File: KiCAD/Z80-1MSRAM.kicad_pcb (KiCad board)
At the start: 2 copper layers, 100 x 75 mm, 36 parts, among them J1 SBC8080 BUS, J2 I/O ADDR SEL, J3 MSX SLOT, Q1 2SC1815, U1 74HC02, U2 74HC74, U3 74HC139, U4 74HC04, U5 74HC00, U6 628128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

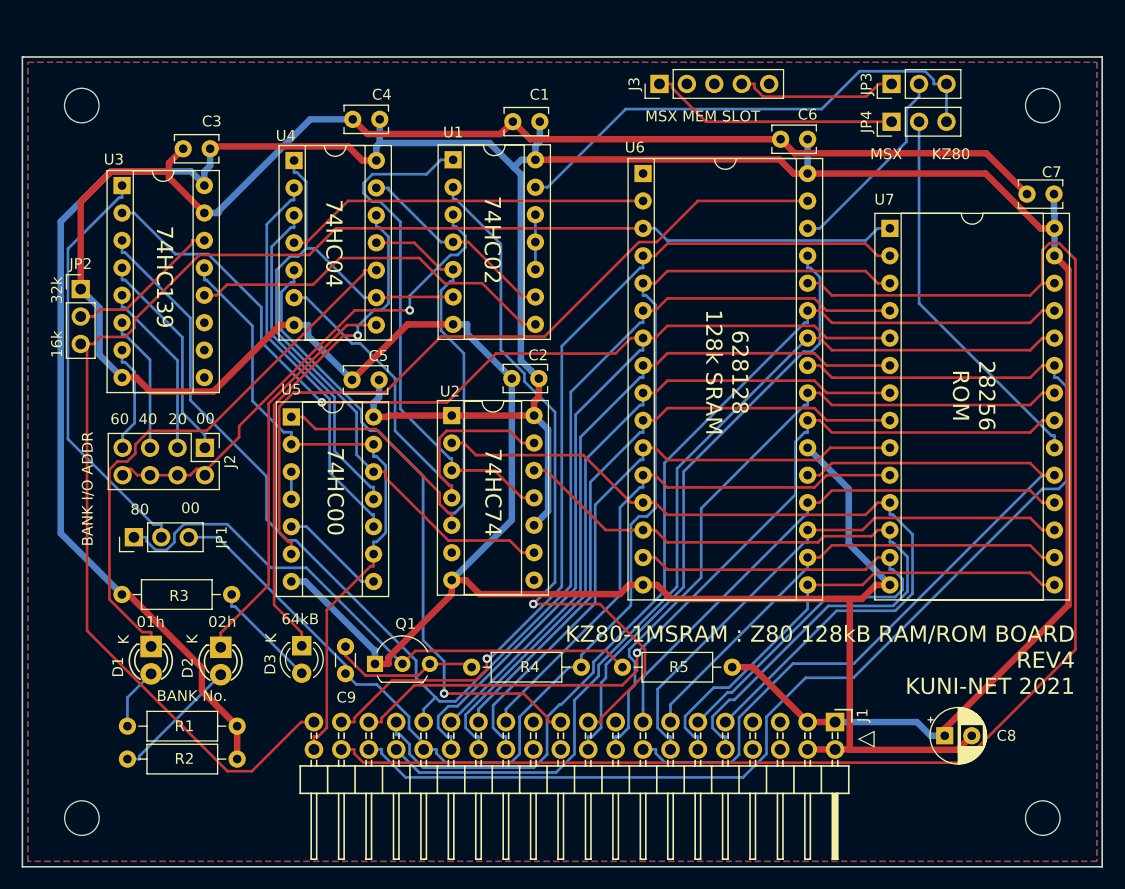
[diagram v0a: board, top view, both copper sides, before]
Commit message: REV4 基板 部品配置変更・ガーバー出力
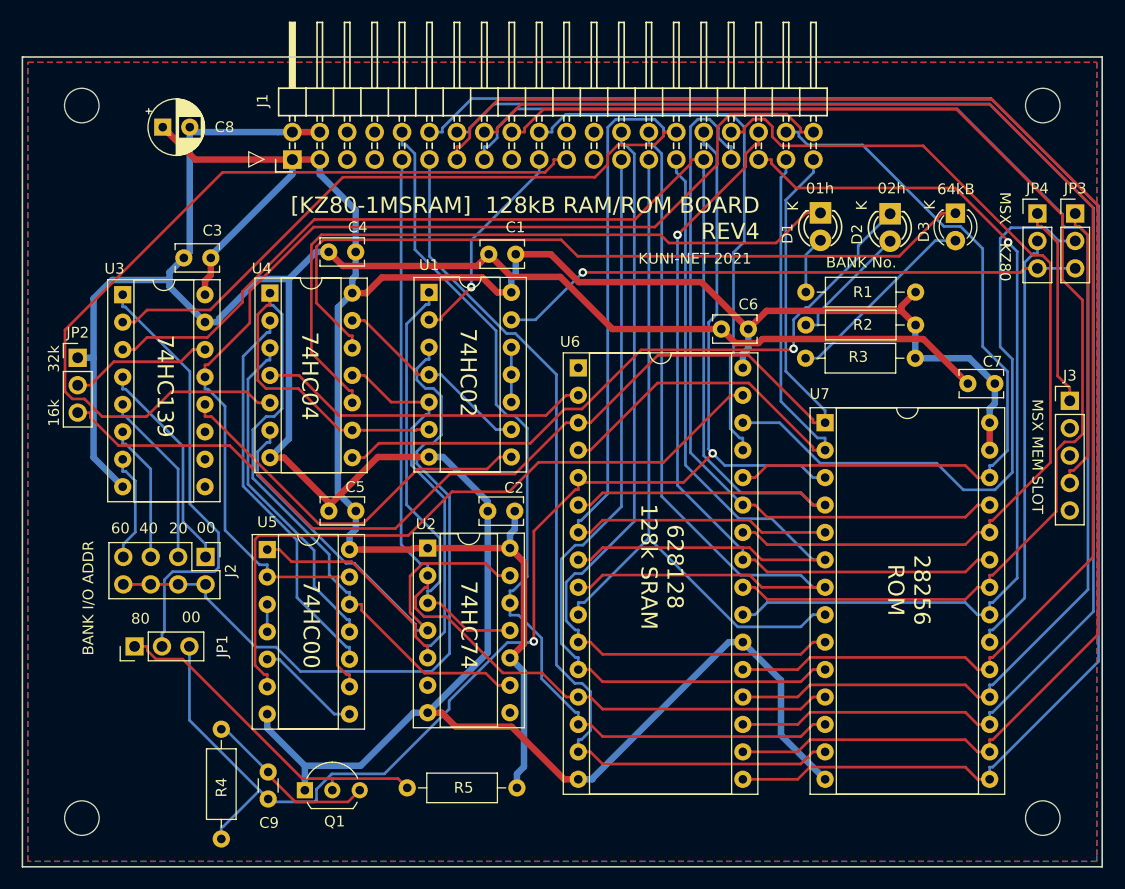
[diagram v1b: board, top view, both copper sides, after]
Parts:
- moved C8 91.8 mm to (113.0, 66.5)
- moved R3 76.7 mm to (182.7, 87.9), turned to 180 degrees
- moved R1 74.6 mm to (182.7, 81.8)
- moved R2 74.6 mm to (182.7, 84.8)
- moved D1 73.9 mm to (173.9, 74.4)
- moved D2 73.9 mm to (180.4, 74.5)
- moved D3 72.6 mm to (186.4, 74.5)
- moved J1 72.4 mm to (125.0, 69.5), turned to 90 degrees
- moved J3 48.0 mm to (197.0, 91.8), turned to 0 degrees
- moved R4 23.9 mm to (118.4, 122.3), turned to 270 degrees
- moved R5 22.9 mm to (135.6, 127.7)
- moved JP3 20.8 mm to (197.5, 74.5), turned to 0 degrees
- moved U6 19.0 mm to (151.5, 88.8)
- moved U7 19.0 mm to (174.3, 93.9)
- moved C6 18.4 mm to (167.2, 85.2)
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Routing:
- net /D3: track 45.3 -> 148.8 mm
- net VCC: track 301.2 -> 198.0 mm
- net /D4: track 44.4 -> 145.7 mm
- net /D5: track 50.7 -> 140.0 mm
- net /D6: track 50.5 -> 135.0 mm
- net /A13: track 140.0 -> 69.7 mm
- net /D7: track 75.6 -> 132.3 mm
- net ~MEMRD: track 65.0 -> 119.4 mm
- net /A15: track 60.0 -> 111.7 mm
- net ~IOWR: track 65.2 -> 19.7 mm
- net /A11: track 114.4 -> 69.4 mm, vias 0 -> 1
- net Net-(JP3-Pad2): track 18.3 -> 58.2 mm
- net /D2: track 51.5 -> 86.3 mm
- net /A12: track 84.1 -> 57.4 mm, vias 1 -> 0
- net Net-(D3-Pad1): track 47.1 -> 72.6 mm, vias 1 -> 0
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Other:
- board text added: "KUNI-NET 2021"
- board text added: "[KZ80-1MSRAM] 128kB RAM/ROM BOARD REV4"
- board text removed: "KZ80-1MSRAM : Z80 128kB RAM/ROM BOARD REV4 KUNI-NET 2021"

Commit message: 基板パターン 縁から離す対応・ガーバー出力
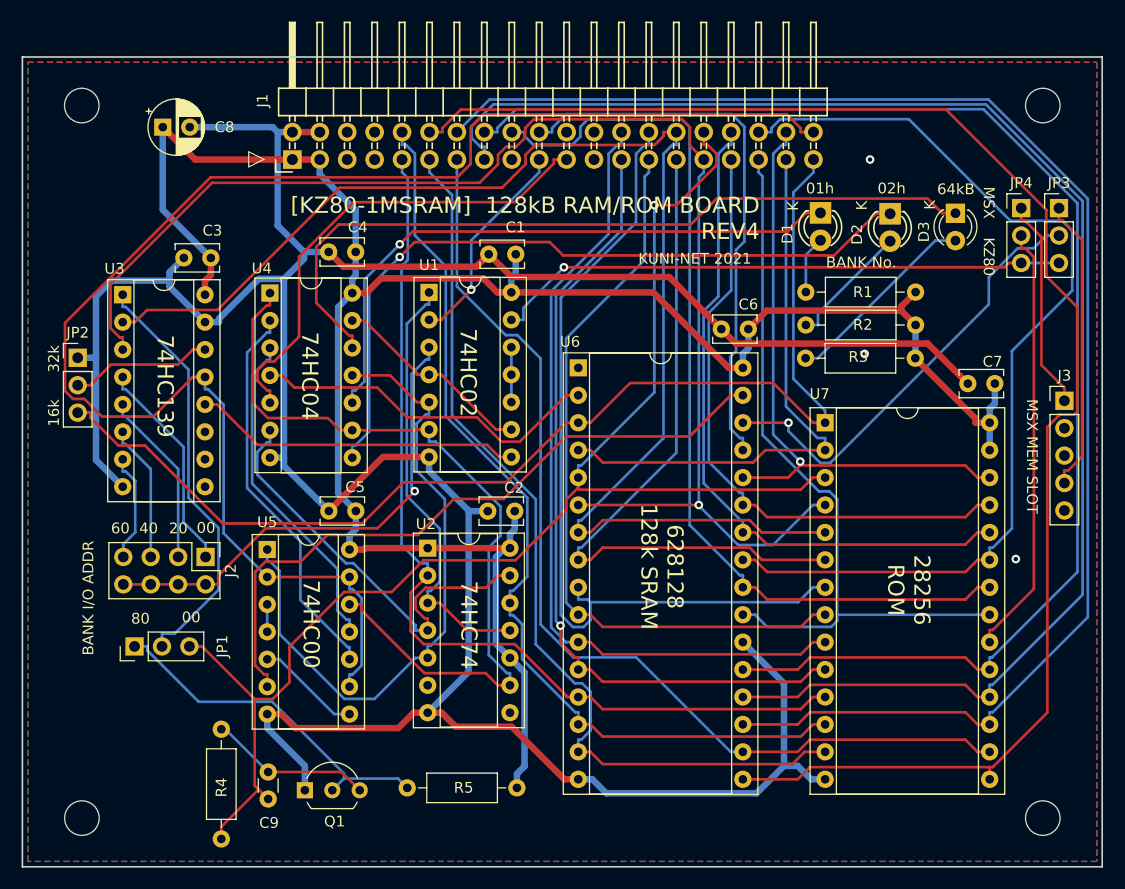
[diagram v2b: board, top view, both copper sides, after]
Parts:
- moved JP3 1.58 mm to (196.0, 74.0)
- moved JP4 1.58 mm to (192.5, 74.0)
- moved J3 0.50 mm to (196.5, 91.8)
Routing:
- net /D4: track 145.7 -> 94.3 mm
- net RES: track 80.2 -> 44.9 mm
- net ~MEMRD: track 119.4 -> 87.6 mm
- net /A15: track 111.7 -> 142.1 mm
- net /A9: track 87.6 -> 63.8 mm
- net Net-(J2-Pad2): track 67.9 -> 45.3 mm, vias 0 -> 1
- net /A11: track 69.4 -> 91.6 mm, vias 1 -> 0
- net Net-(JP3-Pad2): track 58.2 -> 41.5 mm, vias 0 -> 1
- net /A10: track 86.4 -> 69.9 mm, vias 1 -> 0
- net /A13: track 69.7 -> 56.4 mm, vias 0 -> 1
- net /A8: track 67.7 -> 58.1 mm
- net Net-(D1-Pad1): track 65.4 -> 56.8 mm, vias 0 -> 1
- net Net-(D2-Pad1): track 61.4 -> 68.7 mm
- net Net-(U1-Pad8): track 36.2 -> 30.4 mm
- net /DA0: track 55.0 -> 60.6 mm
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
